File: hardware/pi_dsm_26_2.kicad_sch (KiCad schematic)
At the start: 17 parts, among them J1 Conn_Plug_3P_Protected, J2 Conn_Receptacle_3P_Protected, J3 Terra da chapa - terminal olh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, K1 Módulo relé 5V - controle, K1b1 Módulo relé 5V - contatos, SW1 SW_Push

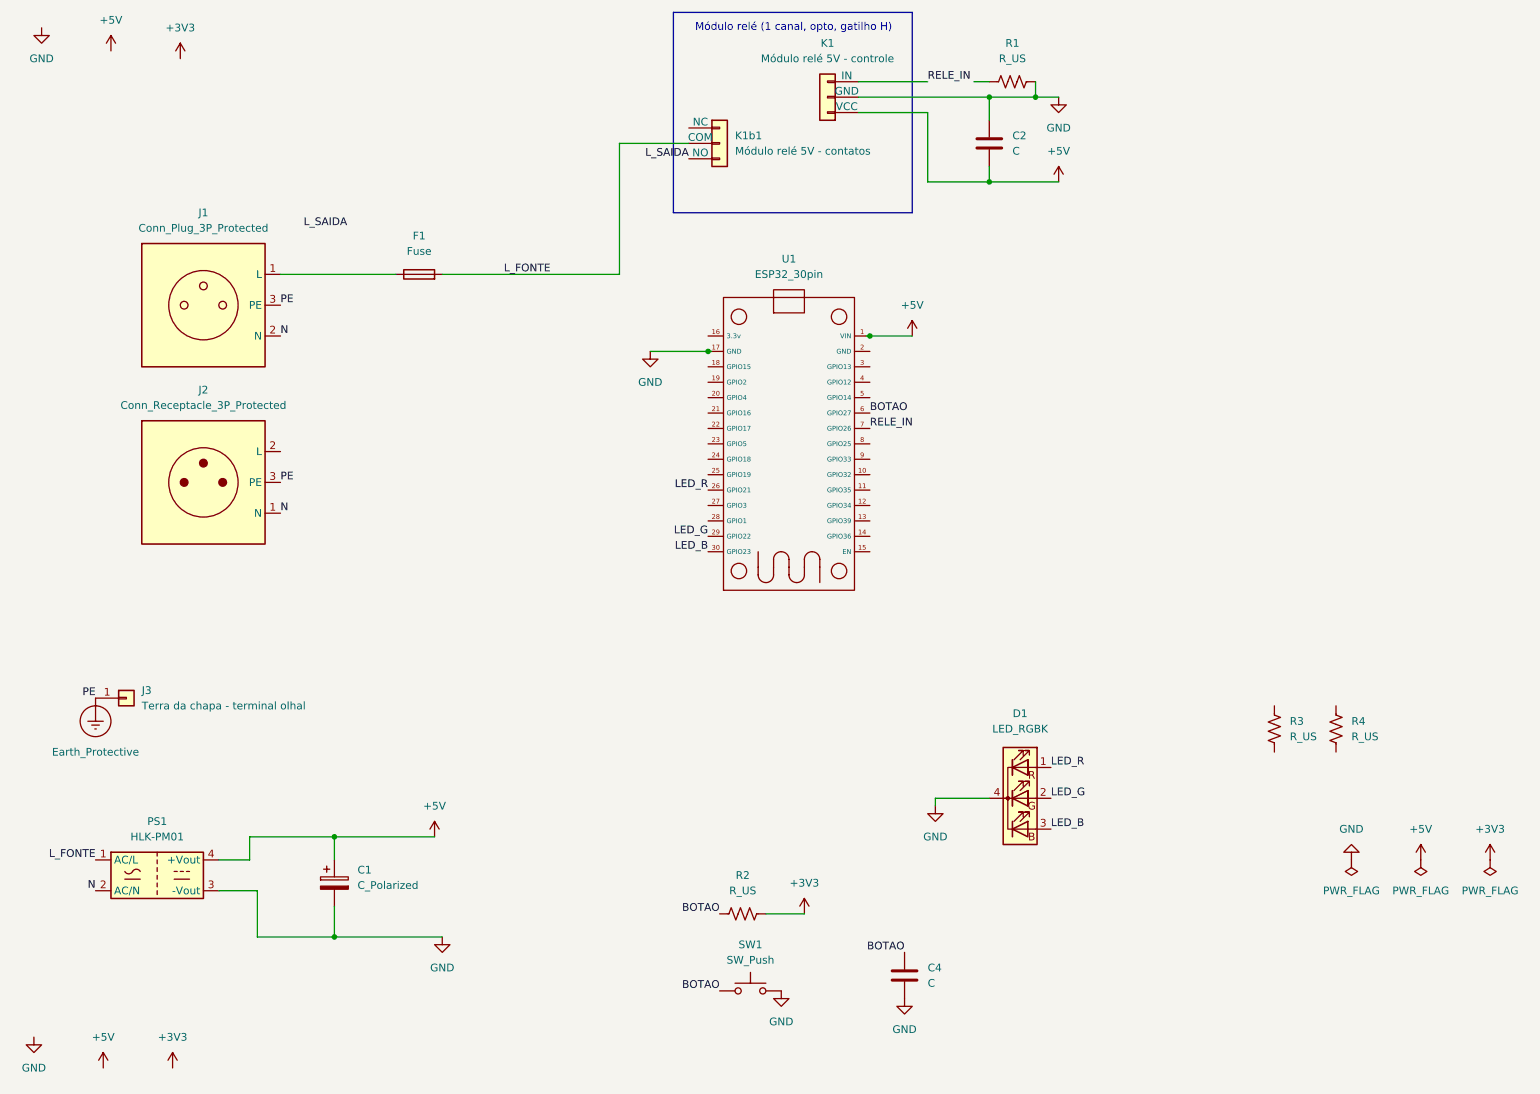
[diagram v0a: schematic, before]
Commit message: Corrige conexões do esquemático conforme especificação de componentes
Reescreve hardware/pi_dsm_26_2.kicad_sch com a pinagem e as ligações da
especificação de componentes:

- J1/J2 -> Conn_01x03, PS1 -> Conn_01x04; K1b1 mantido (ref "K1b" é
  inválida no KiCad, precisa terminar em dígito)
- R_US -> R, adiciona R5; valores: R1/R2 10k, R3 220R, R4/R5 100R,
  C1 470uF/16V, C2/C4 100nF, F1 10A/250V
- Fecha ligações que faltavam: fase chaveada K1b1(NO) -> J2 -> cafeteira,
  resistores de série de cada cor do LED RGB (D1 cátodo comum),
  R1 de RELE_IN a GND, GND do pino 17 do ESP32
- VIN e 3V3 do símbolo esp32_30pin passam a power_in para não colidir
  com os PWR_FLAG de +5V/+3V3
- title block: rev A e data

ERC (kicad-cli 10.0.5): 21 pinos não conectados nos GPIOs livres do U1
(esperados) + 1 aviso de PWR_FLAG. Netlist conferida.

Co-Authored-By: Claude Sonnet 5 <noreply@anthropic.com>
Claude-Session: https://claude.ai/code/session_01Eqrwdkgtbvq6K73DvDBeXT
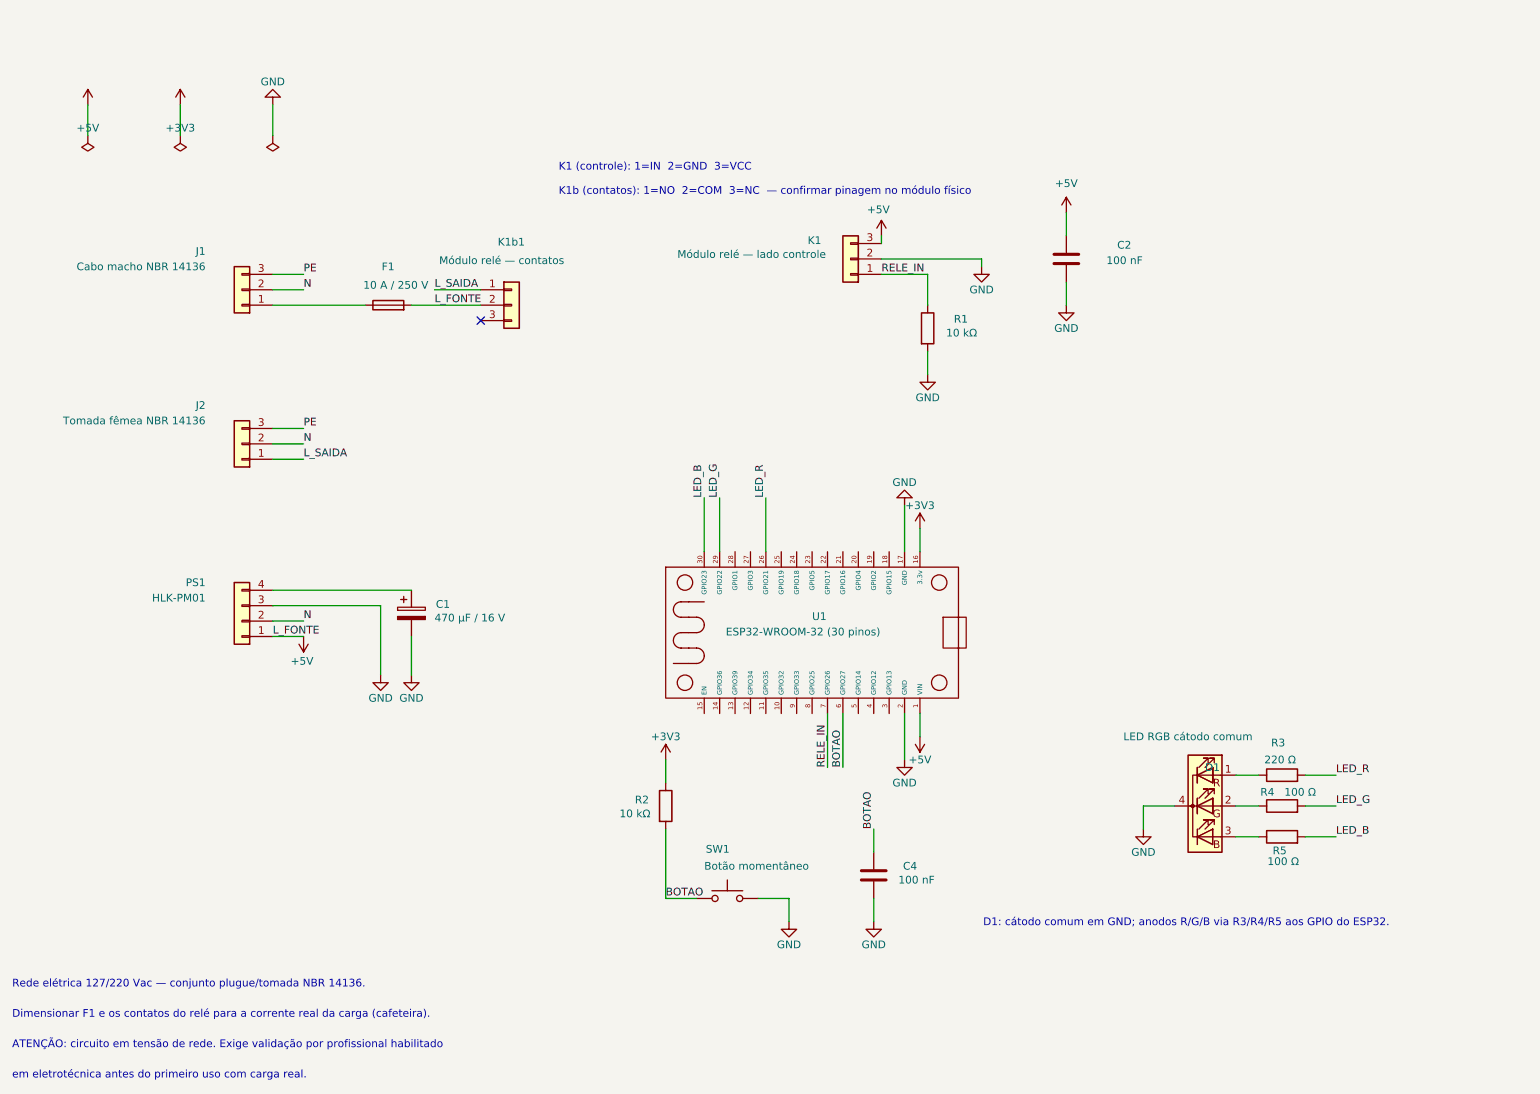
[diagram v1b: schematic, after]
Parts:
- removed J1: Conn_Plug_3P_Protected, symbol Connector:Conn_Plug_3P_Protected
- removed J2: Conn_Receptacle_3P_Protected, symbol Connector:Conn_Receptacle_3P_Protected
- removed J3: Terra da chapa - terminal olhal, symbol Connector_Generic:Conn_01x01
- removed PS1: HLK-PM01, Converter_ACDC:Converter_ACDC_Hi-Link_HLK-PMxx, symbol Converter_ACDC:HLK-PM01
- removed R1, R2, R3, R4: R_US, symbol Device:R_US
- added J1: Cabo macho NBR 14136, symbol Connector_Generic:Conn_01x03
- added J2: Tomada fêmea NBR 14136, symbol Connector_Generic:Conn_01x03
- added PS1: HLK-PM01, symbol Connector_Generic:Conn_01x04
- added R1, R2: 10 kΩ, symbol Device:R
- added R3: 220 Ω, symbol Device:R
- added R4, R5: 100 Ω, symbol Device:R
- C1: value C_Polarized -> 470 µF / 16 V
- C2, C4: value C -> 100 nF
- D1: value LED_RGBK -> LED RGB cátodo comum
- F1: value Fuse -> 10 A / 250 V
- K1: value Módulo relé 5V - controle -> Módulo relé — lado controle
- K1b1: value Módulo relé 5V - contatos -> Módulo relé — contatos
- SW1: value SW_Push -> Botão momentâneo
- U1: value (none) -> ESP32-WROOM-32 (30 pinos); footprint ESP32_30pin -> (none)
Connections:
- net L_FONTE is gone; now on net +5V: F1.2, K1b1.2 (Pin_2)
- net +3V3: now also U1.16 (3.3v), R2.1
- net +5V: now also C2.1, K1.3 (Pin_3), PS1.1 (Pin_1); no longer C1.1, C2.2, K1.1 (VCC)
- net BOTAO: now also R2.2
- net GND: now also C2.2, U1.2 (GND), PS1.3 (Pin_3), R1.2; no longer C2.1
- net LED_B: now also R5.2; no longer D1.3 (BA)
- net LED_G: now also R4.2; no longer D1.2 (GA)
- net LED_R: now also R3.2; no longer D1.1 (RA)
- net L_SAIDA: now also K1b1.1 (Pin_1), J2.1 (Pin_1); no longer K1b1.3 (NO)
- net N: now also J1.2 (Pin_2), J2.2 (Pin_2), PS1.2 (Pin_2)
- net RELE_IN: now also K1.1 (Pin_1), R1.1; no longer K1.3 (IN)
- net at F1.1: now also J1.1 (Pin_1)
- new net: D1.2 (GA), R4.1
- new net: C1.1, PS1.4 (Pin_4)
- new net: D1.3 (BA), R5.1
- new net: D1.1 (RA), R3.1
- new net PE: J1.3 (Pin_3), J2.3 (Pin_3)
- no-connect marks 0 -> 1
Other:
- note added: "ATENÇÃO: circuito em tensão de rede. Exige validação por profissional habilitado"
- note added: "D1: cátodo comum em GND; anodos R/G/B via R3/R4/R5 aos GPIO do ESP32."
- note added: "Dimensionar F1 e os contatos do relé para a corrente real da carga (cafeteira)."
- note added: "K1 (controle): 1=IN 2=GND 3=VCC"
- note added: "K1b (contatos): 1=NO 2=COM 3=NC — confirmar pinagem no módulo físico"
- note added: "Rede elétrica 127/220 Vac — conjunto plugue/tomada NBR 14136."
- note added: "em eletrotécnica antes do primeiro uso com carga real."
- note removed: "Módulo relé (1 canal, opto, gatilho H)"
- title: Base IoT - Cafeteira Conectada (Cafey) -> Base IoT — Cafeteira Conectada

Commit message: Revisa esquematico: simbolos dedicados, terra da chapa e correcoes
- PS1->U2 (Converter_ACDC:HLK-PM01), plugue/tomada como
  Conn_Plug/Receptacle_3P_Protected (P1/J1), rele num simbolo unico
  relay_module:Relay_Module_1CH (K3, biblioteca do projeto)
- Restaura J3 (terminal olhal) + simbolo Earth_Protective no no de terra
  da chapa de aco; rede PE renomeada para Earth_Protective (P1.PE, J1.PE, J3)
- Corrige fiacao do plugue de entrada (fase/neutro/terra estavam trocados);
  PWR_FLAG em L_REDE e L_SAIDA
- Preenche campos de Valor de P1, J1 e K3; fecha buraco de numeracao C4->C3
- Netlist conferida no a no com kicad-cli; ERC limpo salvo GPIOs livres do
  U1 e duas exclusoes documentadas (passagem N/terra plugue->tomada)
- STATUS.md alinhado as referencias atuais

Co-Authored-By: Claude Sonnet 5 <noreply@anthropic.com>
Claude-Session: https://claude.ai/code/session_01BHiTY75Gn8gRCHQYpufdy4
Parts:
- removed J1: Cabo macho NBR 14136, symbol Connector_Generic:Conn_01x03
- removed J2: Tomada fêmea NBR 14136, symbol Connector_Generic:Conn_01x03
- removed K1: Módulo relé — lado controle, symbol Connector_Generic:Conn_01x03
- removed K1b1: Módulo relé — contatos, symbol Connector_Generic:Conn_01x03
- removed PS1: HLK-PM01, symbol Connector_Generic:Conn_01x04
- added J1: Tomada fêmea NBR 14136, symbol Connector:Conn_Receptacle_3P_Protected
- added J3: Terra da chapa de aço — terminal olhal, symbol Connector_Generic:Conn_01x01
- added K3: Módulo relé 5 V, 1 canal, gatilho alto, symbol relay_module:Relay_Module_1CH
- added P1: Cabo macho NBR 14136, symbol Connector:Conn_Plug_3P_Protected
- added U2: HLK-PM01, Converter_ACDC:Converter_ACDC_Hi-Link_HLK-PMxx, symbol Converter_ACDC:HLK-PM01
- U1: value ESP32-WROOM-32 (30 pinos) -> ESP32 DevKit V1 (30 pinos)
- renumbered C4 to C3
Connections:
- net +5V: now also C1.1, K3.3 (VCC), U2.4 (+Vout); no longer F1.2
- net GND: now also K3.2 (GND), U2.3 (-Vout)
- net L_SAIDA: now also J1.2 (L), K3.5 (NO)
- net N: now also J1.1 (N), P1.2 (N), U2.2 (AC/N)
- net RELE_IN: now also K3.1 (IN)
- net L_REDE: now reaches F1.1
- net L_REDE: now also P1.1 (L)
- new net Earth_Protective: J1.3 (PE), J3.1 (Pin_1), P1.3 (PE)
- new net L_FONTE: F1.2, K3.4 (COM), U2.1 (AC/L)
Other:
- note removed: "K1 (controle): 1=IN 2=GND 3=VCC"
- note removed: "K1b (contatos): 1=NO 2=COM 3=NC — confirmar pinagem no módulo físico"
- moved on the sheet: C1, R1

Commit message: fix(hardware): relé active-low, R1 pull-up e F1 10 A T
Alinha o esquemático com o firmware e o módulo de relé real (HL-52S,
2 canais, gatilho de nível BAIXO):

- K3: "1 canal, gatilho alto" -> "2 canais (1 em uso), gatilho baixo"
- R1 passa de pull-down (GND) para pull-up (+3V3): com o GPIO em alta
  impedância no boot, IN fica em ALTO = relé desligado (estado seguro)
- F1: "10 A / 250 V" -> "10 A T / 250 V" (retardado; protege a carga e
  o contato do relé, decisão de manter a filosofia do esquemático)
- J3: valor atualizado para borne de aterramento DIN (gabinete plástico
  FDM, sem massa metálica a aterrar)

ERC re-rodado com kicad-cli 10.0.5: 0 erros, 22 avisos esperados
(21 GPIOs livres + 1 pin_to_pin U1.GND<->U2.-Vout). Netlist reconferida.
PDF regenerado.

Co-Authored-By: Claude Sonnet 5 <noreply@anthropic.com>
Claude-Session: https://claude.ai/code/session_01XgsUFq8XijzcQTgGTtFGmd
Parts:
- F1: value 10 A / 250 V -> 10 A T / 250 V
- J3: value Terra da chapa de aço — terminal olhal -> Borne de aterramento DIN verde-amarelo — PE passa-através (rede->tomada); gabinete plástico FDM, sem massa metálica a a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
- K3: value Módulo relé 5 V, 1 canal, gatilho alto -> Módulo relé 5 V, 2 canais (1 em uso), gatilho baixo (HL-52S, LOW=liga)
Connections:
- net +3V3: now also R1.2
- net GND: no longer R1.2
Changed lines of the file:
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@@
 			)
 		)
-		(property "Value" "Módulo relé 5 V, 1 canal, gatilho alto"
+		(property "Value" "Módulo relé 5 V, 2 canais (1 em uso), gatilho baixo (HL-52S, LOW=liga)"
 			(at 111.76 48.26 0)
 			(show_name no)
@@
 	)
 	(symbol
-		(lib_id "power:GND")
-		(at 134.62 82.55 0)
+		(lib_id "power:+3V3")
+		(at 134.62 82.55 180)
 		(unit 1)
 		(body_style 1)
@@
 			)
 		)
-		(property "Value" "GND"
+		(property "Value" "+3V3"
 			(at 134.62 86.36 0)
 			(show_name no)
@@
 			)
 		)
-		(property "Value" "10 A / 250 V"
+		(property "Value" "10 A T / 250 V"
 			(at 86.614 62.738 90)
 			(show_name no)
@@
 			)
 		)
-		(property "Value" "Terra da chapa de aço — terminal olhal"
+		(property "Value" "Borne de aterramento DIN verde-amarelo — PE passa-através (rede->tomada); gabinete plástico FDM, sem massa metálica a aterrar"
 			(at 39.37 132.0799 0)
 			(show_name no)
